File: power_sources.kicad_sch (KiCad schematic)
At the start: 10 parts, among them J3 5 V in: 2S-6S BEC or 1S BMS/b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, J4 USB_C_PROGRAM_POWER, U3 LM66100DCKR, U5 LM66100DCKR

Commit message: Schematic review: TPS2121 input stage, DS-009 ports, sequencing and CS fixes; docs trimmed
Datasheet-grounded review of the full flight-controller schematic. Downstream
of the input everything verified pin-by-pin (TPS62913, TPS7A20, RP2354B,
BMI088/BMP581/ADXL375, W25Q128, microSD, PWM). The 5 V input stage did not:

- LM66100 (5.5 V rec-op / 6 V abs-max) replaced by one TPS2121 mux (U25):
  BEC priority on IN1, OV lockout ~5.86 V, current limit ~1.5 A, reverse
  blocking on both inputs, source status on GPIO39. Input spec 4.75-5.5 V.
- 5V_IN: 2x4.7 uF + 100 uF + SMAJ5.0A TVS; J3 JST-XH -> XT30PW-M (pin 1 GND).
- J6/J7/J9 reordered to Pixhawk DS-009 (VCC/sig/sig/GND); GPS/ELRS VCC 5 V.
- VIN_SENSE 22k/10k (full scale 10.6 V, was saturating at 5.5 V).
- TPS7A20 EN <- PWR_GOOD so V3V3_ANA rises after V3V3_SYS.
- RP2354B VREG_AVDD moved to V3V3_SYS (datasheet 6.1.8: must power up with
  VREG_VIN); ADC_AVDD stays on V3V3_ANA.
- 10k pull-ups on the four sensor chip-selects.
- ERC "global label appears once" re-enabled (0 hits).

Generator, netlist checker and SPICE decks updated (TPS2121 behavioral model,
new over-voltage and 2S mis-plug corners). Build idempotent, 143 pin mappings
PASS, ERC 0/0, all corners PASS.

Docs: POWER_*.md history removed, rationale folded into DESIGN_SPEC Decisions;
808 -> 290 lines across README, DESIGN_SPEC, LIBRARIES, simulations/README.

Co-Authored-By: Claude Fable 5.1 <noreply@anthropic.com>
Claude-Session: https://claude.ai/code/session_015cFNiWgf35VN2T43HaK8PE
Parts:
- removed R15, R17: 100k status pullup, Resistor_SMD:R_0603_1608Metric, symbol Device:R
- removed U3, U5: LM66100DCKR, Package_TO_SOT_SMD:SOT-363_SC-70-6, symbol MARV_Power:LM66100_OR
- added C67, C68: 4.7u / 10 V X7R, J3 bulk, Capacitor_SMD:C_0805_2012Metric, symbol Device:C
- added C69: 100u / 10 V polymer, J3 bulk, Capacitor_Tantalum_SMD:CP_EIA-7343-31_Kemet-D, symbol Device:C
- added C70: 100n / 16 V X7R, SS soft-start, Capacitor_SMD:C_0805_2012Metric, symbol Device:C
- added C71: 100n / 16 V X7R, IN1 bypass at U25, Capacitor_SMD:C_0805_2012Metric, symbol Device:C
- added C72: 100n / 16 V X7R, IN2 bypass at U25, Capacitor_SMD:C_0805_2012Metric, symbol Device:C
- added D23: SMAJ5.0A, 5.0 V standoff uni-directional TVS, Diode_SMD:D_SMA, symbol Diode:SMAJ5.0A
- added R42: 32.4k / 1%, PR1 top (5V_IN), Resistor_SMD:R_0603_1608Metric, symbol Device:R
- added R43: 10k / 1%, PR1 bottom, Resistor_SMD:R_0603_1608Metric, symbol Device:R
- added R44: 45.3k / 1%, OV1 top (5V_IN), Resistor_SMD:R_0603_1608Metric, symbol Device:R
- added R45: 10k / 1%, OV1 bottom, Resistor_SMD:R_0603_1608Metric, symbol Device:R
- added R46: 80.6k / 1%, ILM -> 1.49 A, Resistor_SMD:R_0603_1608Metric, symbol Device:R
- added R47: 10k / 1%, ST pull-up (open drain), Resistor_SMD:R_0603_1608Metric, symbol Device:R
- added U25: TPS2121RUXR, Package_DFN_QFN:Texas_VQFN-HR-12_2x2.5mm_P0.5mm, symbol MARV_Power:TPS2121RUX
- C16: value 100n / 16 V -> 100n / 16 V X7R, J3 HF bypass
- J3: value 5 V in: 2S-6S BEC or 1S BMS/boost module, 3 A -> 5 V IN, 4.75-5.5 V, XT30 (BEC/BMS/boost module); footprint Connector_JST:JST_XH_B2B-XH-A_1x02_P2.50mm_Vertical -> Connector_AMASS:AMASS_XT30PW-M_1x02_P2.50mm_Horizontal
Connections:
- net 5V_IN: now also J3.2 (Pin_2), C67.1, C68.1, C69.1, C71.1, D23.1 (A1), R42.1, R44.1, U25.7 (IN1); no longer J3.1 (Pin_1)
- net GND: now also J3.1 (Pin_1), C67.2, C68.2, C69.2, C70.2, C71.2, C72.2, D23.2 (A2), R43.2, R45.2, R46.2, U25.12 (GND), U25.3 (CP2), U25.4 (OV2); no longer J3.2 (Pin_2)
- net USB_VBUS: now also C72.1, U25.2 (IN2)
- net V5_SYS: now also U25.1 (OUT), U25.8 (OUT)
- new net PWR_SRC_ST: R47.2, U25.9 (ST)
- new net U25_ILM: R46.1, U25.10 (ILM)
- new net U25_OV1: R44.2, R45.1, U25.5 (OV1)
- new net U25_PR1: R42.2, R43.1, U25.6 (PR1)
- new net U25_SS: C70.1, U25.11 (SS)
- new net V3V3_SYS: R47.1
- no-connect marks 4 -> 2
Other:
- note added: "5 V INPUTS ONLY: BEC/boost 4.75-5.5 V (J3), USB VBUS ~5 V (J4). NO RAW CELL INPUT ON THIS BOARD."
- note added: "J3 INPUT NETWORK: C16 100 nF + C67/C68 2 x 4.7 uF X7R + C69 100 uF polymer, and D23 SMAJ5.0A (DO-214AC/SMA) clamping 5V_IN to GND. D23 is a UNI-directional TVS: its KiCad symbol inherits the generic A1/A2 pin names from the SM6T family, but the graphic and the DO-214AC band both put the CATHODE on pin 1, so pin 1 goes to 5V_IN and pin 2 (anode) to GND. 5.0 V standoff / 6.4 V VBR min sits above th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"
- note added: "U25 TPS2121 PRIORITY POWER MUX (TI SLVSEA3F). IN1 = 5V_IN is the priority source, IN2 = USB_VBUS the fallback; OUT = V5_SYS. Reverse-current blocking is always on for BOTH channels (Sec 9.3.6, IRCB 0.2/1/2 A, tRCB 10 us, VRCB 0/25/50 mV), so neither input can be back-fed from V5_SYS or from the other input. RON 56 mOhm typ / 100 mOhm max over temperature (Sec 7.5, VINx >= 5 V). PR1 (Sec 10.2.4.1 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"
- note added: "USB_VBUS feeds U25 IN2 directly; no inrush/current limiting on this sheet. Data ESD protection is on POWER 2. No servo rail connection."
- note removed: "5 V INPUTS ONLY: BEC/boost 4.75-5.25 V (J3), USB VBUS ~5 V (J4). NO RAW CELL INPUT ON THIS BOARD."
- note removed: "CE tied to VOUT for reverse-current blocking (TI Fig.13). Natural highest-voltage OR; no guaranteed priority. BEC/boost tolerance and transients must stay below 5.5 V."
- note removed: "USB_VBUS feeds U5 directly; no inrush/current limiting on this sheet. Data ESD protection is on POWER 2. No servo rail connection."
- title: POWER 1 / 5 V in, USB, source isolation -> POWER 1 / 5 V in, USB, priority power mux
- moved on the sheet: C16, C7, J4, R4, R5

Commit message: Replace BMI088 with ICM-45686; vendor all footprints and 3D models for layout
Sensors: U21 is now the TDK ICM-45686 (single AP_CS on GPIO20 as IMU_CS,
INT1/INT2 on GPIO23/24, GPIO21 spare, R49 dropped, VDD+VDDIO on V3V3_ANA
with 100 nF + 1 uF each). Project-local symbol, footprint and stand-in STEP;
footprint numbering verified against DS-000577 Rev 1.0 Sec 11.2 (CCW, top
view). BMI088_SPI derived-symbol machinery removed from the generator.

Layout readiness: new tools/audit_footprints.py checks every component for
a resolvable footprint and present 3D model (128/128 OK). The seven official
KiCad footprints whose STEP files are absent from kicad-packages3d 10.0.6
are vendored into MARV_Packages.pretty with project-local models in
MARV_Packages.3dshapes: manufacturer STEPs (Coilcraft XGL4030, Molex
104031-0811), EasyEDA model (HRO TYPE-C-31-M-12), FreeCAD-generated bodies
from tools/3d/ (RP2354B QFN-80, TPS62913 RPU0010A, TPS2121 RUX0012A, Amass
XT30PW-M), and KiCad generic stand-ins (BMP581, ADXL375). Model offsets were
derived by measurement and confirmed in a rendered check board.
PROVENANCE.md records source, licence and SHA256 per model; LIBRARIES.md
lists the pre-fab 3D-viewer checks and the unverified dimensions.

Checks: build idempotent, ERC 0/0, check_power_netlist 149 mappings /
128 components, run_power_checks PASS, audit 0 needing action.

Co-Authored-By: Claude Fable 5.1 <noreply@anthropic.com>
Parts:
- J3: footprint Connector_AMASS:AMASS_XT30PW-M_1x02_P2.50mm_Horizontal -> MARV_Packages:AMASS_XT30PW-M_1x02_P2.50mm_Horizontal
- J4: footprint Connector_USB:USB_C_Receptacle_HRO_TYPE-C-31-M-12 -> MARV_Packages:USB_C_Receptacle_HRO_TYPE-C-31-M-12
- U25: footprint Package_DFN_QFN:Texas_VQFN-HR-12_2x2.5mm_P0.5mm -> MARV_Packages:Texas_VQFN-HR-12_2x2.5mm_P0.5mm

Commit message: Physical design: VBAT-in buck, ESC pad row, pad-row IO, 50 mm single-sided board
Power: the FC now takes raw 2-6S VBAT from the MicoAir AM32 4-in-1 ESC pad
row (CURR TX M4 M3 M2 M1 VBAT GND, J3) through an AP63205WU 5 V/2 A buck
(U26, XGL4030-472, 3 x 22 uF) into the existing TPS2121 mux; XT30 and its
TVS removed. VBAT sense 100k/10k (36 V FS) on ADC0, ESC current sense on
ADC2, ESC KISS telemetry on GPIO30.

IO per the physical spec (DESIGN_SPEC "Physical design"): solder pad rows
for GPS/ELRS/MAG (JST-GH removed), DBG and buzzer; 3x4 servo block for
PWM5-8; 2x6 spare-IO block; WS2812C-2020 RGB LED replaces the two discrete
LEDs; buzzer moved off-board to pads; flash socket is the 150-mil SOIC-8
(W25Q64 default, APS6404L PSRAM alternative); four 4.0 mm grommet holes on
the 30.5 mm pattern. Passives moved to 0402/0603 for the single-sided
envelope.

Board: tools/setup_pcb.py regenerates MARV-V2.kicad_pcb from the netlist —
50 x 50 mm, 4-layer JLC 7628 stack-up, net classes incl. a 90 ohm USB pair,
edge-anchored connectors, coarse interior placement, silk pad labels.
DRC leaves only unrouted items. The BMP581 project footprint had its 2-pad
edges at +/-0.5 mm (corner pads overlapped, three nets shorted); corrected
to Bosch Fig. 32 (+/-0.25 mm, 0.20 mm gaps).

Checks: ERC 0/0, 217 pin mappings / 139 components, run_power_checks PASS,
audit 139/139, pcb DRC unrouted-only.

Co-Authored-By: Claude Fable 5.1 <noreply@anthropic.com>
Claude-Session: https://claude.ai/code/session_01U6Ud7JA3CDTJZVcZZr5sx1
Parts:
- removed C16: 100n / 16 V X7R, J3 HF bypass, Capacitor_SMD:C_0805_2012Metric, symbol Device:C
- removed C67, C68: 4.7u / 10 V X7R, J3 bulk, Capacitor_SMD:C_0805_2012Metric, symbol Device:C
- removed C69: 100u / 10 V polymer, J3 bulk, Capacitor_Tantalum_SMD:CP_EIA-7343-31_Kemet-D, symbol Device:C
- removed D23: SMAJ5.0A, 5.0 V standoff uni-directional TVS, Diode_SMD:D_SMA, symbol Diode:SMAJ5.0A
- added C73: 10u / 50 V X7R, VIN bulk, Capacitor_SMD:C_1206_3216Metric, symbol Device:C
- added C74: 100n / 50 V X7R, VIN HF bypass, Capacitor_SMD:C_0603_1608Metric, symbol Device:C
- added C75: 100n / 50 V X7R, bootstrap, Capacitor_SMD:C_0603_1608Metric, symbol Device:C
- added C76, C77: 22u / 25 V X5R, buck COUT, Capacitor_SMD:C_1206_3216Metric, symbol Device:C
- added C80: 22u / 25 V X5R, buck COUT (3rd: >=44 uF after DC-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, Capacitor_SMD:C_1206_3216Metric, symbol Device:C
- added L3: 4.7u, Isat 4.4 A, DCR 31.5 mOhm max (Coilcraft XG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, MARV_Packages:L_Coilcraft_XxL4030, symbol Device:L
- added R52: 100k / 1%, EN to VIN, Resistor_SMD:R_0402_1005Metric, symbol Device:R
- added U26: AP63205WU-7, Package_TO_SOT_SMD:TSOT-23-6, symbol Regulator_Switching:AP63205WU
- C7: value 1u / 10 V -> 1u / 10 V X7R 0603; footprint Capacitor_SMD:C_0805_2012Metric -> Capacitor_SMD:C_0603_1608Metric
- C70, C71, C72: footprint Capacitor_SMD:C_0805_2012Metric -> Capacitor_SMD:C_0402_1005Metric
- J3: value 5 V IN, 4.75-5.5 V, XT30 (BEC/BMS/boost module) -> ESC pads (CURR TX M4 M3 M2 M1 VBAT GND); footprint MARV_Packages:AMASS_XT30PW-M_1x02_P2.50mm_Horizontal -> MARV_Packages:PadRow_1x08_P2.00mm; symbol Connector_Generic:Conn_01x02 -> Connector_Generic:Conn_01x08
- R4, R42, R43, R44, R45, R46, R47, R5: footprint Resistor_SMD:R_0603_1608Metric -> Resistor_SMD:R_0402_1005Metric
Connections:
- net 5V_IN: now also C76.1, C77.1, C80.1, L3.2, U26.1 (FB); no longer J3.2 (Pin_2)
- net GND: now also J3.8 (Pin_8), C73.2, C74.2, C76.2, C77.2, C80.2, U26.4 (GND); no longer J3.1 (Pin_1)
- new net CURR_SENSE_RAW: J3.1 (Pin_1)
- new net ESC_TELEM: J3.2 (Pin_2)
- new net PWM1: J3.6 (Pin_6)
- new net PWM2: J3.5 (Pin_5)
- new net PWM3: J3.4 (Pin_4)
- new net PWM4: J3.3 (Pin_3)
- new net U26_BST: C75.1, U26.6 (BST)
- new net U26_EN: R52.2, U26.2 (EN)
- new net U26_SW: C75.2, L3.1, U26.5 (SW)
- new net VBAT: C73.1, C74.1, J3.7 (Pin_7), R52.1, U26.3 (IN)
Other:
- note added: "BOARD INPUTS: VBAT 6-25.2 V (2-6S) from the ESC pad row J3, and USB VBUS ~5 V (J4). U26 (AP63205WU) makes 5V_IN from VBAT; 5V_IN is the priority input of the U25 power mux and also the servo 5 V bus."
- note added: "ESC PAD ROW J3 (MicoAir AM32 4-in-1 ESC, FC-connection row). Order is the ESC silkscreen read left to right: 1 CURR - analog current sense from the ESC, 12.75 mV/A, 0-3.3 V -> R53/C78 -> GPIO42 (ADC2) on BOARD 1. 2 TX - KISS ESC telemetry, 3.3 V, 115200 baud, ESC output only -> R54 -> GPIO30 (PIO UART RX). 3-6 M4 M3 M2 M1 - 3.3 V DShot/PWM inputs, straight from the RP2354B (PWM4..PWM1 = GPIO5, 4,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"
- note added: "U26 AP63205WU-7 VBAT BUCK (Diodes DS41326 Rev. 2-2). 3.8-32 V in, FIXED 5.0 V out (4.95/5.00/5.05 V, Electrical Characteristics VFB row), 2 A, 1.1 MHz with +/-6% frequency spread spectrum, 4 ms internal soft-start, 22 uA quiescent, TSOT-23-6. VIN abs max 35 V DC / 40 V for 400 ms vs a 25.2 V 6S pack. Component values are Table 3 "Recommended Component Selections for AP63205" and Figure 21 verbati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"
- note added: "USB_VBUS feeds U25 IN2 directly; no inrush or current limiting on this sheet. Data ESD protection is on POWER 2. No servo rail connection."
- note removed: "5 V INPUTS ONLY: BEC/boost 4.75-5.5 V (J3), USB VBUS ~5 V (J4). NO RAW CELL INPUT ON THIS BOARD."
- note removed: "J3 INPUT NETWORK: C16 100 nF + C67/C68 2 x 4.7 uF X7R + C69 100 uF polymer, and D23 SMAJ5.0A (DO-214AC/SMA) clamping 5V_IN to GND. D23 is a UNI-directional TVS: its KiCad symbol inherits the generic A1/A2 pin names from the SM6T family, but the graphic and the DO-214AC band both put the CATHODE on pin 1, so pin 1 goes to 5V_IN and pin 2 (anode) to GND. 5.0 V standoff / 6.4 V VBR min sits above th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"
- note removed: "USB_VBUS feeds U25 IN2 directly; no inrush/current limiting on this sheet. Data ESD protection is on POWER 2. No servo rail connection."
- title: POWER 1 / 5 V in, USB, priority power mux -> POWER 1 / ESC pad row, VBAT buck, USB, priority power mux

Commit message: Remove buzzer; passives to 0201/0402; GPIO28 to spare-IO block
Buzzer pads J15, driver Q20/D22/R33/R34 and the BUZZ nets removed; GPIO28
now terminates on J16 pin 12 (was a second GND). Resistors 0201, caps
<= 4.7 uF 0402, 22 uF/10 V 0603, 22 uF/25 V and 10 uF/50 V 0805, 47 uF
0805; USB net-class clearance 0.18 mm so the 0201 series resistors on the
pair pass DRC. Board regenerated at 50 x 50 mm (courtyard fill 63.5 %);
DRC unrouted-only. 134 components, 105 nets; ERC 0/0, 213 pin mappings,
run_power_checks PASS, audit 134/134.

Co-Authored-By: Claude Fable 5.1 <noreply@anthropic.com>
Claude-Session: https://claude.ai/code/session_01U6Ud7JA3CDTJZVcZZr5sx1
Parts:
- C7: value 1u / 10 V X7R 0603 -> 1u / 10 V X7R 0402; footprint Capacitor_SMD:C_0603_1608Metric -> Capacitor_SMD:C_0402_1005Metric
- C73: value 10u / 50 V X7R, VIN bulk -> 10u / 50 V X5R 0805 GRM21BR61H106KE43, VIN bulk; footprint Capacitor_SMD:C_1206_3216Metric -> Capacitor_SMD:C_0805_2012Metric
- C74: value 100n / 50 V X7R, VIN HF bypass -> 100n / 50 V X7R 0402, VIN HF bypass; footprint Capacitor_SMD:C_0603_1608Metric -> Capacitor_SMD:C_0402_1005Metric
- C75: value 100n / 50 V X7R, bootstrap -> 100n / 50 V X7R 0402, bootstrap; footprint Capacitor_SMD:C_0603_1608Metric -> Capacitor_SMD:C_0402_1005Metric
- C76, C77: value 22u / 25 V X5R, buck COUT -> 22u / 25 V X5R 0805 GRM21BR61E226ME44, buck COUT; footprint Capacitor_SMD:C_1206_3216Metric -> Capacitor_SMD:C_0805_2012Metric
- C80: value 22u / 25 V X5R, buck COUT (3rd: >=44 uF after DC-bias derating, AP63205 EVB guide) -> 22u / 25 V X5R 0805 GRM21BR61E226ME44, buck COUT (3rd: >=44 uF after DC-bias derating, AP63205 EVB guide); footprint Capacitor_SMD:C_1206_3216Metric -> Capacitor_SMD:C_0805_2012Metric
- R4, R42, R43, R44, R45, R46, R47, R5, R52: footprint Resistor_SMD:R_0402_1005Metric -> Resistor_SMD:R_0201_0603Metric

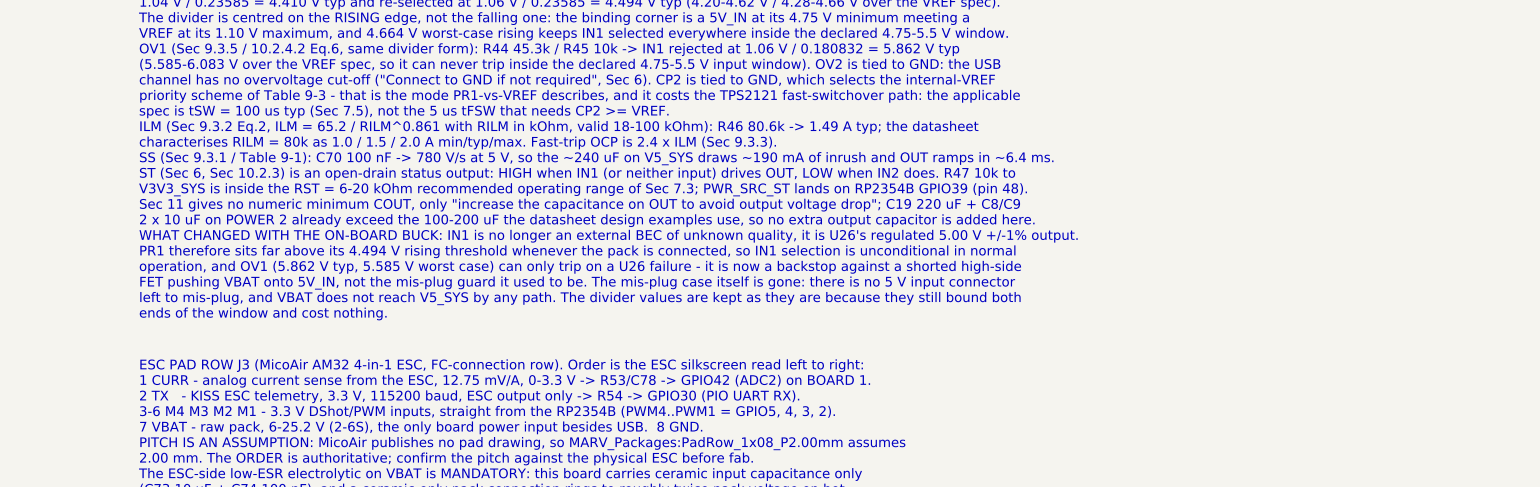
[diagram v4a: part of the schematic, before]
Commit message: Flash socket becomes an optional back-side expansion; ESC row on the back edge; C19 100 uF
U24 (SOIC-8 150 mil) and its caps C62/C63 are DNP, excluded from the BOM
and placed flipped on the back with a legend ("FLASH / PSRAM EXPANSION,
SOIC-8 150mil, QMI CS1, W25Q64JVSSIQ or APS6404L-3SQR-SN"); the RP2354B's
internal 2 MB flash and the microSD cover firmware and logging. The ESC pad
row J3 sits along the left edge on the back, like the DBG row on the bottom
edge. C19 (V5_SYS bulk) reduced from 220 uF D-case to 100 uF 6.3 V B-case:
the ngspice decks now use CPOLY=100u and every handover predicate still
passes (worst-case V5_SYS min 4.37 V). Board 46.6 x 41.2 mm; DRC
unrouted-only; ERC 0/0, checker PASS, audit 140/140.

Co-Authored-By: Claude Fable 5.1 <noreply@anthropic.com>
Claude-Session: https://claude.ai/code/session_01U6Ud7JA3CDTJZVcZZr5sx1
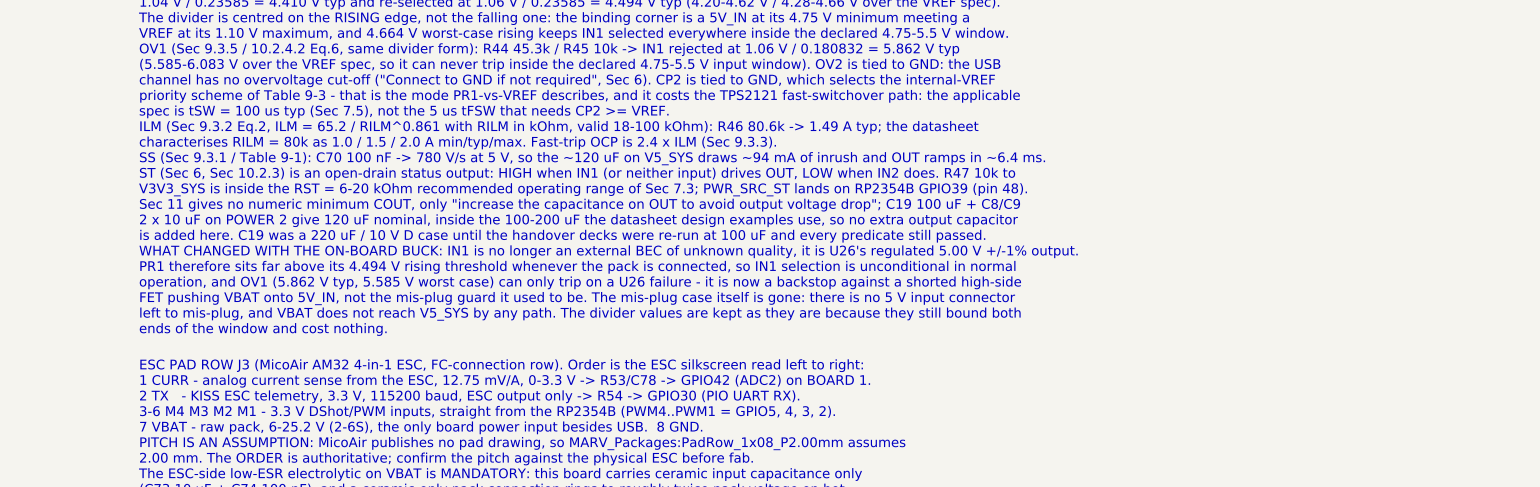
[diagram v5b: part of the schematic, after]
